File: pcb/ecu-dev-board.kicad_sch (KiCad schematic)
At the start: 2 parts, among them J1 MX23A18NF1, J2 39-30-1020

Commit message: removed GNDPWR
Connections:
- net GNDPWR renamed GND
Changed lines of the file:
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@@
-	)
-	(symbol
-		(lib_id "power:GNDPWR")
-		(at 46.99 166.37 270)
-		(unit 1)
-		(exclude_from_sim no)
-		(in_bom yes)
-		(on_board yes)
-		(dnp no)
-		(fields_autoplaced yes)
-		(property "Reference" "#PWR057"
-			(at 41.91 166.37 0)
-			(effects
-				(font
-					(size 1.27 1.27)
-				)
-				(hide yes)
-			)
-		)
-		(property "Value" "GNDPWR"
-			(at 43.18 166.2429 90)
-			(effects
-				(font
-					(size 1.27 1.27)
-				)
-				(justify right)
-			)
-		)
-		(property "Footprint" ""
-			(at 45.72 166.37 0)
-			(effects
-				(font
-					(size 1.27 1.27)
-				)
-				(hide yes)
-			)
-		)
-		(property "Datasheet" ""
-			(at 45.72 166.37 0)
-			(effects
-				(font
-					(size 1.27 1.27)
-				)
-				(hide yes)
-			)
-		)
-		(property "Description" "Power symbol creates a global label with name \"GNDPWR\" , global ground"
-			(at 46.99 166.37 0)
-			(effects
-				(font
-					(size 1.27 1.27)
-				)
-				(hide yes)
-			)
-		)
-		(pin "1"
-		)
-		(instances
-			(project "ecu-dev-board"
-				(path "/38d4df77-b5a0-4642-8410-8b13c21c2c3b"
-					(reference "#PWR057")
-					(unit 1)
-				)
-			)
-		)
 	)
 	(symbol
@@
 					(unit 1)
 				)
+			)
+		)
+	)
+	(symbol
+		(lib_id "power:GND")
+		(at 46.99 166.37 270)
+		(unit 1)
+		(exclude_from_sim no)
+		(in_bom yes)
+		(on_board yes)
+		(dnp no)
+		(property "Reference" "#PWR049"
+			(at 40.64 166.37 0)
+			(effects
+				(font
+					(size 1.27 1.27)
+				)
+				(hide yes)
+			)
+		)
+		(property "Value" "GND"
+			(at 38.862 166.116 90)
+			(effects
+				(font
+					(size 1.27 1.27)
+				)
+				(justify left)
+			)
+		)
+		(property "Footprint" ""
+			(at 46.99 166.37 0)
+			(effects
+				(font
+					(size 1.27 1.27)
+				)
+				(hide yes)
+			)
+		)
+		(property "Datasheet" ""
+			(at 46.99 166.37 0)
+			(effects
+				(font
+					(size 1.27 1.27)
+				)
+				(hide yes)
+			)
+		)
+		(property "Description" "Power symbol creates a global label with name \"GND\" , ground"
+			(at 46.99 166.37 0)
+			(effects
+				(font
+					(size 1.27 1.27)
+				)
+				(hide yes)
+			)
+		)
+		(pin "1"
+		)
+		(instances
+			(project "ecu-dev-board"
+				(path "/38d4df77-b5a0-4642-8410-8b13c21c2c3b"
+					(reference "#PWR049")
+					(unit 1)
+				)

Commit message: revision 2.0: added LC Vbatt filtering and changed Pmos protection to be a schttoky
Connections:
- net +12V renamed +BATT
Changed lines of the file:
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@@
-	)
-	(symbol
-		(lib_id "power:+12V")
-		(at 46.99 168.91 90)
-		(unit 1)
-		(exclude_from_sim no)
-		(in_bom yes)
-		(on_board yes)
-		(dnp no)
-		(fields_autoplaced yes)
-		(property "Reference" "#PWR059"
-			(at 50.8 168.91 0)
-			(effects
-				(font
-					(size 1.27 1.27)
-				)
-				(hide yes)
-			)
-		)
-		(property "Value" "+12V"
-			(at 43.18 168.9099 90)
-			(effects
-				(font
-					(size 1.27 1.27)
-				)
-				(justify left)
-			)
-		)
-		(property "Footprint" ""
-			(at 46.99 168.91 0)
-			(effects
-				(font
-					(size 1.27 1.27)
-				)
-				(hide yes)
-			)
-		)
-		(property "Datasheet" ""
-			(at 46.99 168.91 0)
-			(effects
-				(font
-					(size 1.27 1.27)
-				)
-				(hide yes)
-			)
-		)
-		(property "Description" "Power symbol creates a global label with name \"+12V\""
-			(at 46.99 168.91 0)
-			(effects
-				(font
-					(size 1.27 1.27)
-				)
-				(hide yes)
-			)
-		)
-		(pin "1"
-		)
-		(instances
-			(project ""
-				(path "/38d4df77-b5a0-4642-8410-8b13c21c2c3b"
-					(reference "#PWR059")
-					(unit 1)
-				)
-			)
-		)
 	)
 	(symbol
@@
 					(unit 1)
 				)
+			)
+		)
+	)
+	(symbol
+		(lib_id "power:+BATT")
+		(at 46.99 168.91 90)
+		(unit 1)
+		(exclude_from_sim no)
+		(in_bom yes)
+		(on_board yes)
+		(dnp no)
+		(property "Reference" "#PWR059"
+			(at 50.8 168.91 0)
+			(effects
+				(font
+					(size 1.27 1.27)
+				)
+				(hide yes)
+			)
+		)
+		(property "Value" "+BATT"
+			(at 40.386 169.164 90)
+			(effects
+				(font
+					(size 1.27 1.27)
+				)
+			)
+		)
+		(property "Footprint" ""
+			(at 46.99 168.91 0)
+			(effects
+				(font
+					(size 1.27 1.27)
+				)
+				(hide yes)
+			)
+		)
+		(property "Datasheet" ""
+			(at 46.99 168.91 0)
+			(effects
+				(font
+					(size 1.27 1.27)
+				)
+				(hide yes)
+			)
+		)
+		(property "Description" "Power symbol creates a global label with name \"+BATT\""
+			(at 46.99 168.91 0)
+			(effects
+				(font
+					(size 1.27 1.27)
+				)
+				(hide yes)
+			)
+		)
+		(pin "1"
+		)
+		(instances
+			(project "ecu-dev-board"
+				(path "/38d4df77-b5a0-4642-8410-8b13c21c2c3b"
+					(reference "#PWR059")
+					(unit 1)
+				)

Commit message: revision 2.0: changed components numeration
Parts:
- renumbered J1 to J101, J2 to J102
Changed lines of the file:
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@@
 		(dnp no)
 		(fields_autoplaced yes)
-		(property "Reference" "J1"
+		(property "Reference" "J101"
 			(at 67.31 156.21 0)
 			(effects
@@
 			(project "ecu-dev-board"
 				(path "/38d4df77-b5a0-4642-8410-8b13c21c2c3b"
-					(reference "J1")
+					(reference "J101")
 					(unit 1)
 				)
@@
 		(on_board yes)
 		(dnp no)
-		(property "Reference" "J2"
+		(property "Reference" "J102"
 			(at 120.904 160.02 0)
 			(effects
@@
 			(project ""
 				(path "/38d4df77-b5a0-4642-8410-8b13c21c2c3b"
-					(reference "J2")
+					(reference "J102")
 					(unit 1)
 				)
@@
 		(on_board yes)
 		(dnp no)
-		(property "Reference" "#PWR049"
+		(property "Reference" "#PWR0101"
 			(at 40.64 166.37 0)
 			(effects
@@
 			(project "ecu-dev-board"
 				(path "/38d4df77-b5a0-4642-8410-8b13c21c2c3b"
-					(reference "#PWR049")
+					(reference "#PWR0101")
 					(unit 1)
 				)
@@
 		(on_board yes)
 		(dnp no)
-		(property "Reference" "#PWR059"
+		(property "Reference" "#PWR0102"
 			(at 50.8 168.91 0)
 			(effects
@@
 			(project "ecu-dev-board"
 				(path "/38d4df77-b5a0-4642-8410-8b13c21c2c3b"
-					(reference "#PWR059")
+					(reference "#PWR0102")
 					(unit 1)
 				)

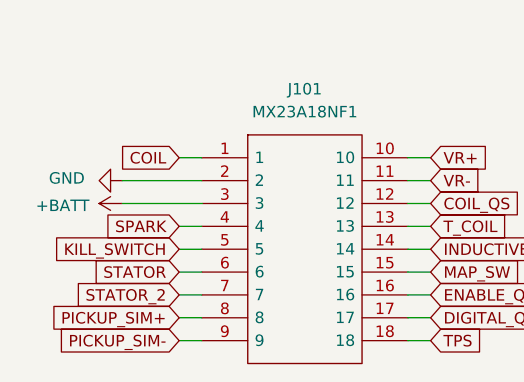
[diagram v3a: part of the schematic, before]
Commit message: moved ac-dc converter
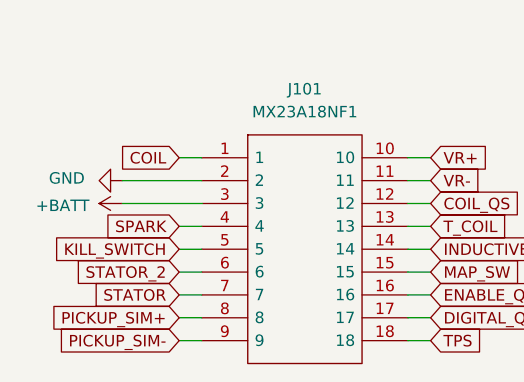
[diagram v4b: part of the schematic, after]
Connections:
- net STATOR: now also J101.7; no longer J101.6
- net STATOR_2: now also J101.6; no longer J101.7
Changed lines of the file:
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@@
 	(global_label "STATOR"
 		(shape input)
-		(at 53.34 176.53 180)
+		(at 53.34 179.07 180)
 		(fields_autoplaced yes)
 		(effects
@@
 		)
 		(property "Intersheetrefs" "${INTERSHEET_REFS}"
-			(at 43.521 176.53 0)
+			(at 41.3439 179.07 0)
 			(effects
 				(font
@@
 	(global_label "STATOR_2"
 		(shape input)
-		(at 53.34 179.07 180)
+		(at 53.34 176.53 180)
 		(fields_autoplaced yes)
 		(effects
@@
 		)
 		(property "Intersheetrefs" "${INTERSHEET_REFS}"
-			(at 41.3439 179.07 0)
+			(at 43.521 176.53 0)
 			(effects
 				(font

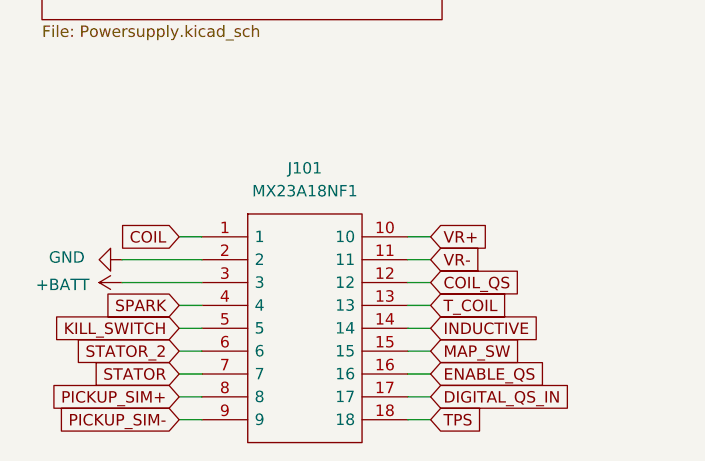
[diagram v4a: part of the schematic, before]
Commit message: changed battery pin with coil qs
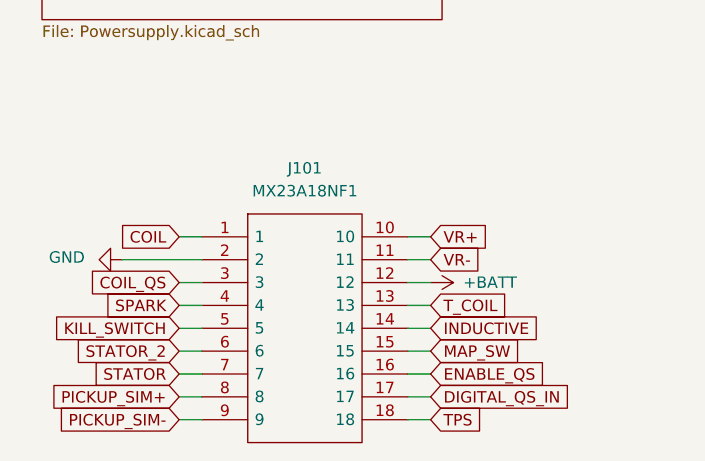
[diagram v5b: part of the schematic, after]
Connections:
- net +BATT: now also J101.12; no longer J101.3
- net COIL_QS: now also J101.3; no longer J101.12
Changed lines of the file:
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@@
 	(wire
 		(pts
-			(xy 46.99 168.91) (xy 55.88 168.91)
+			(xy 53.34 168.91) (xy 55.88 168.91)
 		)
 		(stroke
@@
 		)
 	)
+	(global_label "COIL_QS"
+		(shape input)
+		(at 53.34 168.91 180)
+		(fields_autoplaced yes)
+		(effects
+			(font
+				(size 1.27 1.27)
+			)
+			(justify right)
+		)
+		(property "Intersheetrefs" "${INTERSHEET_REFS}"
+			(at 42.6138 168.91 0)
+			(effects
+				(font
+					(size 1.27 1.27)
+				)
+				(justify right)
+				(hide yes)
+			)
+		)
+	)
 	(global_label "INDUCTIVE"
 		(shape input)
@@
 				)
 				(justify right)
-				(hide yes)
-			)
-		)
-	)
-	(global_label "COIL_QS"
-		(shape input)
-		(at 81.28 168.91 0)
-		(fields_autoplaced yes)
-		(effects
-			(font
-				(size 1.27 1.27)
-			)
-			(justify left)
-		)
-		(property "Intersheetrefs" "${INTERSHEET_REFS}"
-			(at 92.0062 168.91 0)
-			(effects
-				(font
-					(size 1.27 1.27)
-				)
-				(justify left)
 				(hide yes)
 			)
@@
 	(symbol
 		(lib_id "power:+BATT")
-		(at 46.99 168.91 90)
+		(at 81.28 168.91 270)
 		(unit 1)
 		(exclude_from_sim no)
@@
 		(dnp no)
 		(property "Reference" "#PWR0102"
-			(at 50.8 168.91 0)
+			(at 77.47 168.91 0)
 			(effects
 				(font
@@
 		)
 		(property "Value" "+BATT"
-			(at 40.386 169.164 90)
+			(at 87.884 168.91 90)
 			(effects
 				(font
@@
 		)
 		(property "Footprint" ""
-			(at 46.99 168.91 0)
+			(at 81.28 168.91 0)
 			(effects
 				(font
@@
 		)
 		(property "Datasheet" ""
-			(at 46.99 168.91 0)
+			(at 81.28 168.91 0)
 			(effects
 				(font
@@
 		)
 		(property "Description" "Power symbol creates a global label with name \"+BATT\""
-			(at 46.99 168.91 0)
-			(effects
-				(font
+			(at 81.28 168.91 0)
+			(effects
+				(font
